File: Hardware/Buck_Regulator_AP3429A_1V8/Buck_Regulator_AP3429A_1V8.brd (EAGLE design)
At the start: 25.4 x 25.4 mm, 51 parts, among them J1 Screw Terminal, J2 POWER_JACKPOWER_JACK_SLOT_COM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, J3 Breakout Headers, U1 AP3429/A

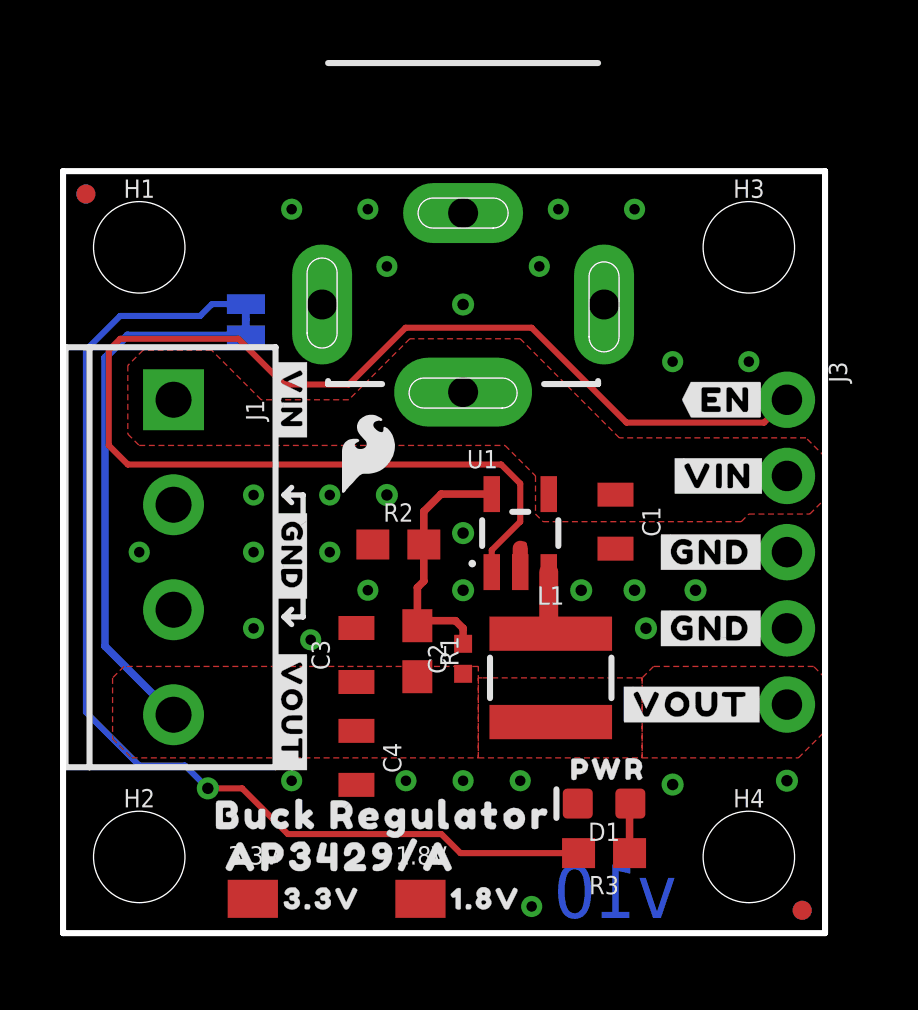
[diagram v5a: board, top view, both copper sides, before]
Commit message: Added 2 more output capacitors
Added more output capacitance to match ALC block - there was some ripple detected during testing so adding these should eliminate that. Adjusted the components on the board accordingly then matched the exact locations of said movement for each board.
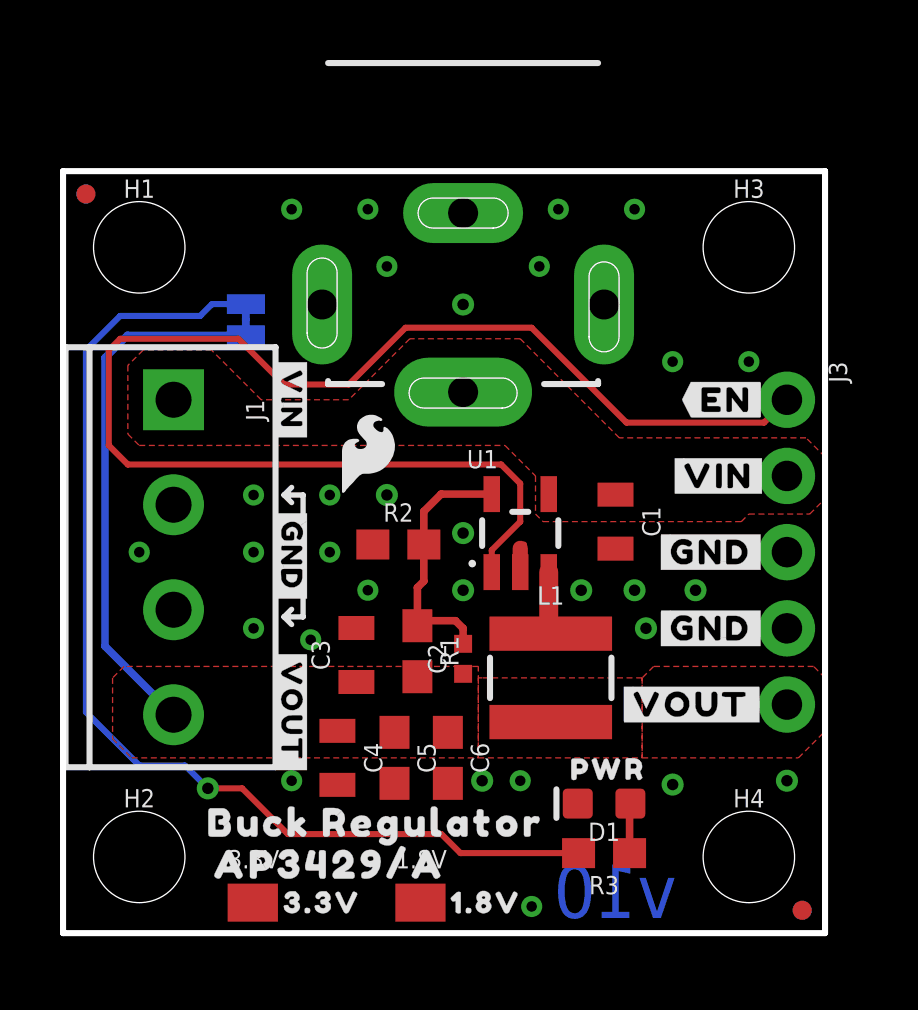
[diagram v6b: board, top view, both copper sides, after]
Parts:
- added C5: 0.1uF, SparkFun-Capacitors:0603
- added C6: 1.0uF, SparkFun-Capacitors:0603
- moved C4 0.63 mm to (9.14, 5.84)
- moved U$3 0.46 mm to (8.89, 2.29)
- moved U$2 0.36 mm to (10.4, 3.68)
- moved 1.8V 0.13 mm to (11.9, 1.02)
- moved 3.3V 0.13 mm to (6.35, 1.02)
- moved U$19 0.13 mm to (14.1, 1.02)
- moved U$23 0.13 mm to (8.64, 1.02)
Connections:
- net GND: now also C5.2, C6.2
- net VOUT: now also C5.1, C6.1
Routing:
- net GND: vias 31 -> 30
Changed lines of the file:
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@@
 <drawing>
 <settings>
-<setting alwaysvectorfont="no"/>
+<setting alwaysvectorfont="yes"/>
 <setting verticaltext="up"/>
 </settings>
@@
 <layer number="37" name="tTest" color="7" fill="1" visible="no" active="yes"/>
 <layer number="38" name="bTest" color="7" fill="1" visible="no" active="yes"/>
-<layer number="39" name="tKeepout" color="4" fill="11" visible="no" active="yes"/>
-<layer number="40" name="bKeepout" color="1" fill="11" visible="no" active="yes"/>
-<layer number="41" name="tRestrict" color="4" fill="10" visible="no" active="yes"/>
-<layer number="42" name="bRestrict" color="1" fill="10" visible="no" active="yes"/>
+<layer number="39" name="tKeepout" color="4" fill="11" visible="yes" active="yes"/>
+<layer number="40" name="bKeepout" color="1" fill="11" visible="yes" active="yes"/>
+<layer number="41" name="tRestrict" color="4" fill="10" visible="yes" active="yes"/>
+<layer number="42" name="bRestrict" color="1" fill="10" visible="yes" active="yes"/>
 <layer number="43" name="vRestrict" color="2" fill="10" visible="no" active="yes"/>
 <layer number="44" name="Drills" color="7" fill="1" visible="no" active="yes"/>
@@
 <attribute name="VALUE" x="22.098" y="19.05" size="0.6096" layer="27" font="vector" ratio="20" rot="R270"/>
 </element>
-<element name="U$2" library="output" package="BUCK_REGULATOR24" value="" x="10.668" y="3.937" smashed="yes"/>
-<element name="U$3" library="output" package="AP3429#A25" value="" x="9.271" y="2.54" smashed="yes"/>
+<element name="U$2" library="output" package="BUCK_REGULATOR24" value="" x="10.414" y="3.683" smashed="yes"/>
+<element name="U$3" library="output" package="AP3429#A25" value="" x="8.89" y="2.286" smashed="yes"/>
 <element name="U$4" library="output" package="#VOUT#3431" value="" x="20.955" y="7.62" smashed="yes"/>
 <element name="U$5" library="output" package="#GND#3432" value="" x="21.59" y="10.16" smashed="yes"/>
@@
 <attribute name="VALUE" x="1.397" y="17.78" size="0.6096" layer="27" font="vector" ratio="20" rot="R270"/>
 </element>
-<element name="3.3V" library="SparkFun-Aesthetics" package="PRODUCT_IDENT_NO_NO-SILK" value="PROD_ID_NO-PASTE_NO_SILK" x="6.35" y="1.143" smashed="yes">
-<attribute name="NAME" x="6.35" y="2.286" size="0.6096" layer="25" font="vector" ratio="20" align="bottom-center"/>
-<attribute name="VALUE" x="6.35" y="0" size="0.6096" layer="27" font="vector" ratio="20" align="top-center"/>
-</element>
-<element name="1.8V" library="SparkFun-Aesthetics" package="PRODUCT_IDENT_PASTE_NO-SILK" value="PROD_ID_PASTE_NO-SILK" x="11.938" y="1.143" smashed="yes">
-<attribute name="NAME" x="11.938" y="2.286" size="0.6096" layer="25" font="vector" ratio="20" align="bottom-center"/>
-<attribute name="VALUE" x="11.938" y="0" size="0.6096" layer="27" font="vector" ratio="20" align="top-center"/>
-</element>
-<element name="U$23" library="output" package="3#3V3441" value="" x="8.636" y="1.143" smashed="yes"/>
-<element name="U$19" library="output" package="1#8V3441" value="" x="14.097" y="1.143" smashed="yes"/>
+<element name="3.3V" library="SparkFun-Aesthetics" package="PRODUCT_IDENT_NO_NO-SILK" value="PROD_ID_NO-PASTE_NO_SILK" x="6.35" y="1.016" smashed="yes">
+<attribute name="NAME" x="6.35" y="2.159" size="0.6096" layer="25" font="vector" ratio="20" align="bottom-center"/>
+<attribute name="VALUE" x="6.35" y="-0.127" size="0.6096" layer="27" font="vector" ratio="20" align="top-center"/>
+</element>
+<element name="1.8V" library="SparkFun-Aesthetics" package="PRODUCT_IDENT_PASTE_NO-SILK" value="PROD_ID_PASTE_NO-SILK" x="11.938" y="1.016" smashed="yes">
+<attribute name="NAME" x="11.938" y="2.159" size="0.6096" layer="25" font="vector" ratio="20" align="bottom-center"/>
+<attribute name="VALUE" x="11.938" y="-0.127" size="0.6096" layer="27" font="vector" ratio="20" align="top-center"/>
+</element>
+<element name="U$23" library="output" package="3#3V3441" value="" x="8.636" y="1.016" smashed="yes"/>
+<element name="U$19" library="output" package="1#8V3441" value="" x="14.097" y="1.016" smashed="yes"/>
 <element name="U$20" library="output" package="PWR3441" value="" x="18.161" y="5.461" smashed="yes"/>
 <element name="U$25" library="output" package="#EN#3443" value="" x="22.098" y="17.78" smashed="yes"/>
@@
 <attribute name="VALUE" x="10.668" y="9.271" size="0.6096" layer="27" font="vector" ratio="20" rot="R90" align="top-center"/>
 </element>
-<element name="C4" library="SparkFun-Capacitors" package="0805" value="22uF" x="9.779" y="5.842" smashed="yes" rot="R270">
-<attribute name="NAME" x="10.668" y="5.842" size="0.6096" layer="25" font="vector" ratio="20" rot="R270" align="bottom-center"/>
-<attribute name="PROD_ID" value="CAP-14260" x="9.779" y="5.842" size="1.778" layer="27" font="vector" ratio="15" rot="R270" display="off"/>
-<attribute name="VALUE" x="8.89" y="5.842" size="0.6096" layer="27" font="vector" ratio="20" rot="R270" align="top-center"/>
+<element name="C4" library="SparkFun-Capacitors" package="0805" value="22uF" x="9.144" y="5.842" smashed="yes" rot="R270">
+<attribute name="NAME" x="10.033" y="5.842" size="0.6096" layer="25" font="vector" ratio="20" rot="R270" align="bottom-center"/>
+<attribute name="PROD_ID" value="CAP-14260" x="9.144" y="5.842" size="1.778" layer="27" font="vector" ratio="15" rot="R270" display="off"/>
+<attribute name="VALUE" x="8.255" y="5.842" size="0.6096" layer="27" font="vector" ratio="20" rot="R270" align="top-center"/>
 </element>
 <element name="U$16" library="output" package="BUCK_REGULATOR_AP3429#A3453" value="" x="1.524" y="12.827" smashed="yes" rot="MR90"/>
 <element name="J2" library="SparkFun-Connectors" package="POWER_JACK_PTH_SLOT_BOTH" value="POWER_JACKPOWER_JACK_SLOT_COMBO" x="13.335" y="24.003" smashed="yes" rot="R90"/>
+<element name="C5" library="SparkFun-Capacitors" package="0603" value="0.1uF" x="11.049" y="5.842" smashed="yes" rot="R270">
+<attribute name="NAME" x="11.811" y="5.842" size="0.6096" layer="25" font="vector" ratio="20" rot="R270" align="bottom-center"/>
+<attribute name="PROD_ID" value="CAP-08604" x="11.049" y="5.842" size="1.778" layer="27" font="vector" ratio="15" rot="R270" display="off"/>
+<attribute name="VALUE" x="10.287" y="5.842" size="0.6096" layer="27" font="vector" ratio="20" rot="R270" align="top-center"/>
+</element>
+<element name="C6" library="SparkFun-Capacitors" package="0603" value="1.0uF" x="12.827" y="5.842" smashed="yes" rot="R270">
+<attribute name="NAME" x="13.589" y="5.842" size="0.6096" layer="25" font="vector" ratio="20" rot="R270" align="bottom-center"/>
+<attribute name="PROD_ID" value="CAP-13930" x="12.827" y="5.842" size="1.778" layer="27" font="vector" ratio="15" rot="R270" display="off"/>
+<attribute name="VALUE" x="12.065" y="5.842" size="0.6096" layer="27" font="vector" ratio="20" rot="R270" align="top-center"/>
+</element>
 </elements>
 <signals>
@@
 <via x="6.35" y="10.16" extent="1-16" drill="0.35"/>
 <via x="15.24" y="5.08" extent="1-16" drill="0.35"/>
-<via x="13.335" y="5.08" extent="1-16" drill="0.35"/>
-<via x="11.43" y="5.08" extent="1-16" drill="0.35"/>
 <via x="7.62" y="5.08" extent="1-16" drill="0.35"/>
 <via x="22.86" y="19.05" extent="1-16" drill="0.35"/>
@@
 <via x="10.16" y="24.13" extent="1-16" drill="0.35"/>
 <contactref element="J2" pad="GND"/>
+<contactref element="C5" pad="2"/>
+<contactref element="C6" pad="2"/>
+<via x="13.97" y="5.08" extent="1-16" drill="0.381"/>
 </signal>
 <signal name="N$1">
@@
 <vertex x="19.304" y="8.509"/>
 </polygon>
+<contactref element="C5" pad="1"/>
+<contactref element="C6" pad="1"/>
 </signal>
 </signals>
